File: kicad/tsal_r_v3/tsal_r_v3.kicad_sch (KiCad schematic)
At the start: 48 parts, among them J1 Conn_01x02_Pin, J2 Conn_01x02_Pin, Q1 MMBT3904, Q3 AO3401A, U1 TLV431BQDBZR, U2 NE555D, U3 B1212, U4 2N7002, U7 LTV-817S

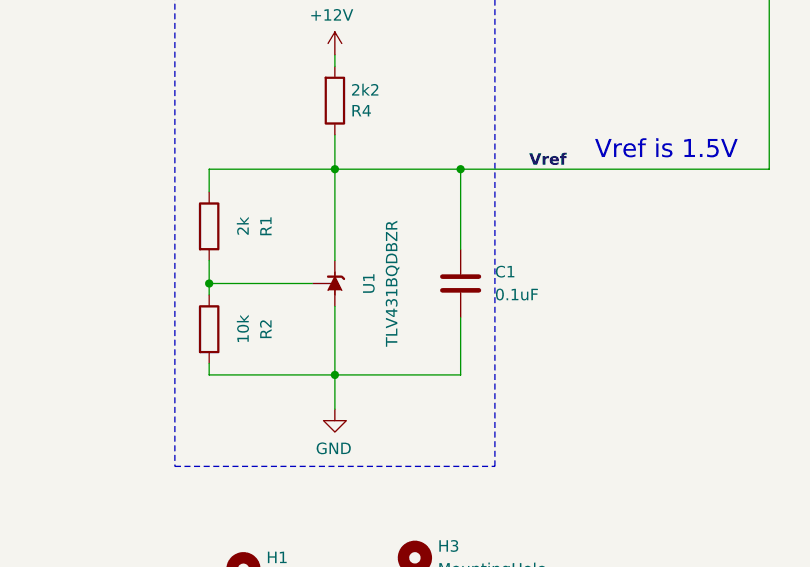
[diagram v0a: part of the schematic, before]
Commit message: TSAL-G v3.0 New PCB design for TSAL-G, with changes for TLV431 for both TSAL-R and TSAL-G
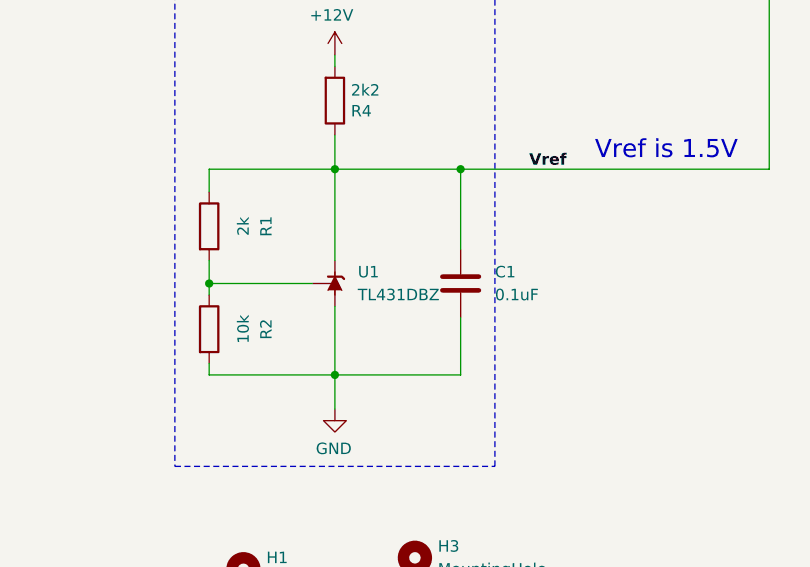
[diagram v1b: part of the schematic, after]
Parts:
- removed U1: TLV431BQDBZR, Package_TO_SOT_SMD:SOT-23, symbol Reference_Voltage:TL431LP
- added U1: TL431DBZ, Package_TO_SOT_SMD:SOT-23, symbol Reference_Voltage:TL431DBZ
- D2: footprint Diode_SMD:D_SMA -> Diode_SMD:D_SMA_Handsoldering
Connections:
- net GND: now also U1.3 (A)
- net Vref: now also U1.1 (K)
- net at R1.2, R2.1: now also U1.2 (REF)

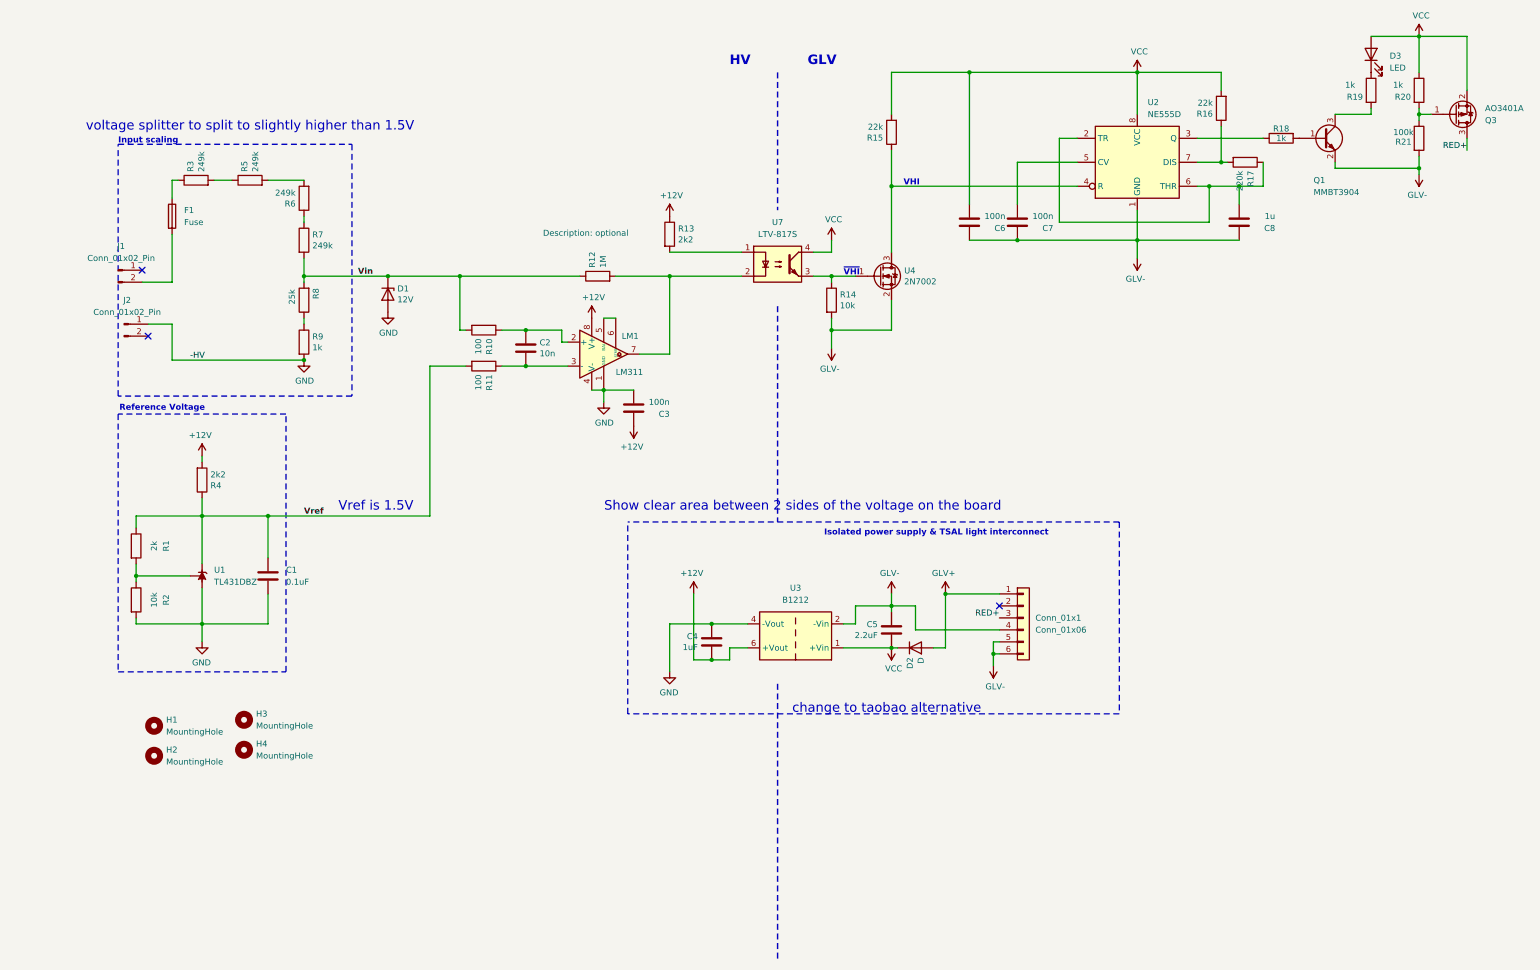
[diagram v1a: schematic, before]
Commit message: change connectors, footprints and new layout
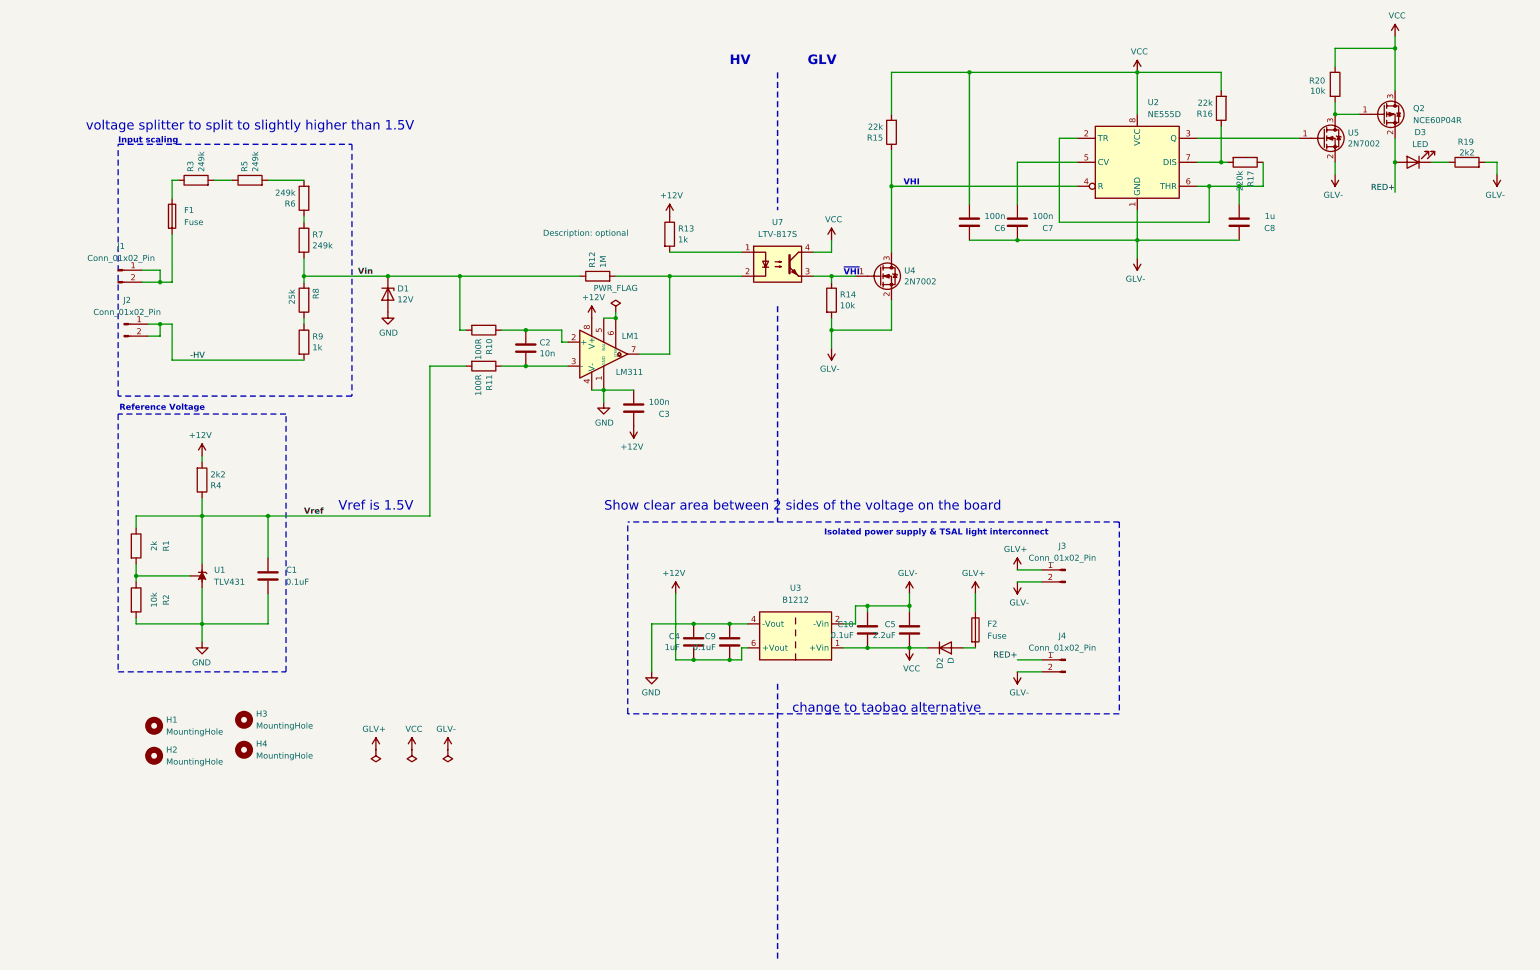
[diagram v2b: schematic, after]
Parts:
- removed Conn_01x1: Conn_01x06, Connector_JST:JST_VH_B6P-VH_1x06_P3.96mm_Vertical, symbol Connector_Generic:Conn_01x06
- removed Q1: MMBT3904, Package_TO_SOT_SMD:SOT-23_Handsoldering, symbol Transistor_BJT:MMBT3904
- removed Q3: AO3401A, Package_TO_SOT_SMD:SOT-23_Handsoldering, symbol Transistor_FET:AO3401A
- removed R18: 1k, Resistor_SMD:R_0805_2012Metric_Pad1.20x1.40mm_HandSolder, symbol Device:R
- removed R21: 100k, Resistor_SMD:R_0805_2012Metric_Pad1.20x1.40mm_HandSolder, symbol Device:R
- added C10, C9: 0.1uF, RMC_Capacitor:C_0805_2012Metric_Pad1.18x1.45mm_HandSolder_L, symbol Device:C
- added F2: Fuse, Fuse:Fuse_1210_3225Metric_Pad1.42x2.65mm_HandSolder, symbol Device:Fuse
- added J3, J4: Conn_01x02_Pin, Connector_Molex:Molex_Micro-Fit_3.0_43650-0200_1x02_P3.00mm_Horizontal, symbol Connector:Conn_01x02_Pin
- added Q2: NCE60P04R, Package_TO_SOT_SMD:SOT-223-3_TabPin2, symbol Transistor_FET:Q_PMOS_GSD
- added U5: 2N7002, RMC_SOT:SOT-23, symbol Transistor_FET:2N7002
- C1, C2, C3, C4, C5, C6, C7, C8: footprint Capacitor_SMD:C_0805_2012Metric_Pad1.18x1.45mm_HandSolder -> RMC_Capacitor:C_0805_2012Metric_Pad1.18x1.45mm_HandSolder_L
- D3: footprint LED_SMD:LED_0805_2012Metric_Pad1.15x1.40mm_HandSolder -> RMC_LED:LED_0805_2012Metric_Pad1.45x1.40mm_HandSolder
- F1: footprint Fuse:Fuse_0805_2012Metric_Pad1.15x1.40mm_HandSolder -> Fuse:Fuse_Littelfuse-NANO2-885
- J1, J2: footprint Connector_AMASS:AMASS_XT60-M_1x02_P7.20mm_Vertical -> Connector_Molex:Molex_Micro-Fit_3.0_43650-0200_1x02_P3.00mm_Horizontal
- LM1, U2: footprint Package_SO:SOIC-8_3.9x4.9mm_P1.27mm -> RMC_SO:SOIC-8_3.9x4.9mm_P1.27mm_RMC_Handsolder
- R1, R12, R14, R15, R16, R17, R2, R3, R4, R5, R6, R7, R8, R9: footprint Resistor_SMD:R_0805_2012Metric_Pad1.20x1.40mm_HandSolder -> RMC_Resistor:R_0805_2012Metric_Pad1.20x1.40mm_HandSolder_L
- R10, R11: value 100 -> 100R; footprint Resistor_SMD:R_0805_2012Metric_Pad1.20x1.40mm_HandSolder -> RMC_Resistor:R_0805_2012Metric_Pad1.20x1.40mm_HandSolder_L
- R13: value 2k2 -> 1k; footprint Resistor_SMD:R_0805_2012Metric_Pad1.20x1.40mm_HandSolder -> RMC_Resistor:R_0805_2012Metric_Pad1.20x1.40mm_HandSolder_L
- R19: value 1k -> 2k2; footprint Resistor_SMD:R_0805_2012Metric_Pad1.20x1.40mm_HandSolder -> RMC_Resistor:R_0805_2012Metric_Pad1.20x1.40mm_HandSolder_L
- R20: value 1k -> 10k; footprint Resistor_SMD:R_0805_2012Metric_Pad1.20x1.40mm_HandSolder -> RMC_Resistor:R_0805_2012Metric_Pad1.20x1.40mm_HandSolder_L
- U1: value TL431DBZ -> TLV431; footprint Package_TO_SOT_SMD:SOT-23 -> RMC_SOT:SOT-23
- U3: footprint Converter_DCDC:Converter_DCDC_TRACO_TBA2-xxxx_Single_THT -> Matthew:DCDC Converter F1212
- U4: footprint Package_TO_SOT_SMD:SOT-23_Handsoldering -> RMC_SOT:SOT-23
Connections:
- net +12V: now also C9.2
- net GLV+: now also F2.1, J3.1 (Pin_1); no longer D2.2 (A)
- net GLV-: now also R19.2, C10.1, J3.2 (Pin_2), J4.2 (Pin_2), U5.2 (S)
- net GND: now also C9.1; no longer J2.1 (Pin_1), R9.2
- net RED+: now also D3.2 (A), J4.1 (Pin_1), Q2.2 (S)
- net VCC: now also C10.2, Q2.3 (D); no longer D3.2 (A)
- net at U2.3 (Q): now also U5.1 (G)
- net at R20.2: now also Q2.1 (G), U5.3 (D)
- net at J1.1 (Pin_1): now also F1.2, J1.2 (Pin_2)
- net -HV: now reaches J2.2 (Pin_2)
- net -HV: now also J2.1 (Pin_1), R9.2
- new net: D2.2 (A), F2.2
- no-connect marks 3 -> 0
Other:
- moved on the sheet: C4, C5, D2, R20

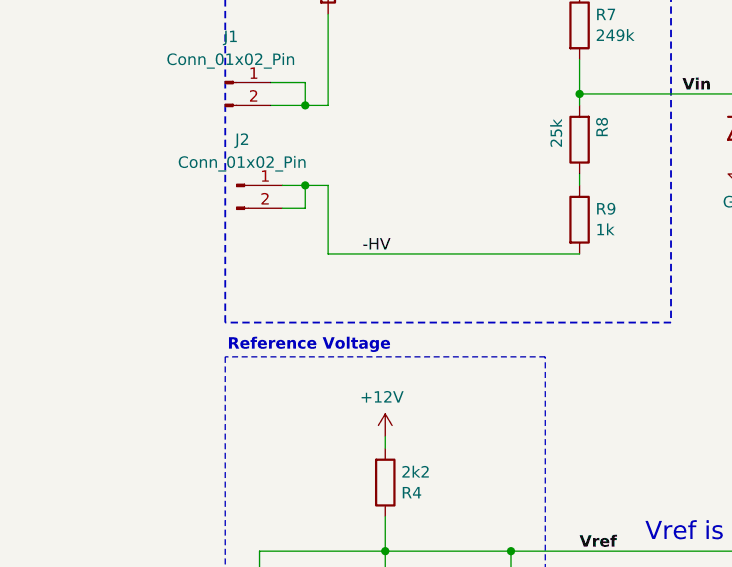
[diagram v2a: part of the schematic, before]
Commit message: Debugged tsal r
inverted tlv431 pad
connected hv- gnd
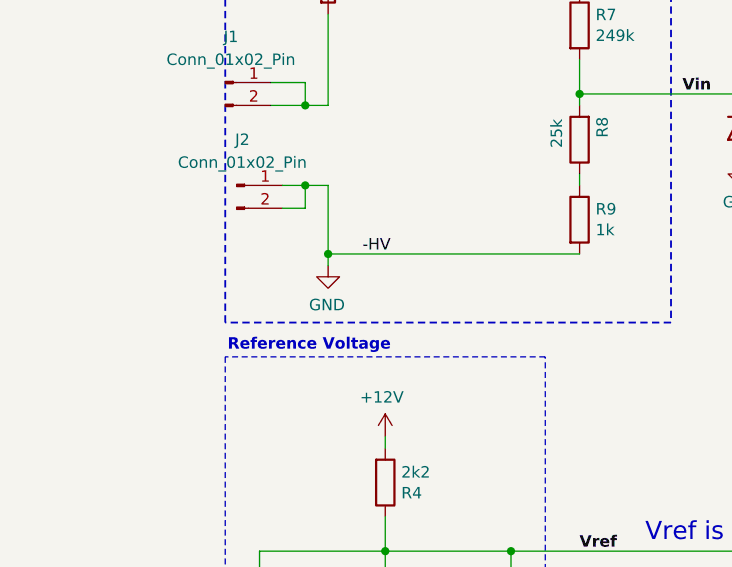
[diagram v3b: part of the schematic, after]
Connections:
- net -HV is gone; now on net GND: J2.1 (Pin_1), J2.2 (Pin_2), R9.2
- net Vref: now also U1.2 (K); no longer U1.1 (K)
- net at R1.2, R2.1: now also U1.1 (REF); no longer U1.2 (REF)
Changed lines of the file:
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@@
 	)
 	(junction
+		(at 72.39 146.05)
+		(diameter 0)
+		(color 0 0 0 0)
+	)
+	(junction
 		(at 228.6 198.12)
 		(diameter 0)
@@
 	(wire
 		(pts
+			(xy 72.39 147.32) (xy 72.39 146.05)
+		)
+		(stroke
+			(width 0)
+			(type default)
+		)
+	)
+	(wire
+		(pts
 			(xy 166.37 135.89) (xy 166.37 137.16)
 		)
@@
 					(unit 1)
 				)
+			)
+		)
+	)
+	(symbol
+		(lib_id "power:GND")
+		(at 72.39 147.32 0)
+		(mirror y)
+		(unit 1)
+		(exclude_from_sim no)
+		(in_bom yes)
+		(on_board yes)
+		(dnp no)
+		(property "Reference" "#PWR026"
+			(at 72.39 153.67 0)
+			(effects
+				(font
+					(size 1.27 1.27)
+				)
+				(hide yes)
+			)
+		)
+		(property "Value" "GND"
+			(at 72.263 151.7142 0)
+			(effects
+				(font
+					(size 1.27 1.27)
+				)
+			)
+		)
+		(property "Footprint" ""
+			(at 72.39 147.32 0)
+			(effects
+				(font
+					(size 1.27 1.27)
+				)
+				(hide yes)
+			)
+		)
+		(property "Datasheet" ""
+			(at 72.39 147.32 0)
+			(effects
+				(font
+					(size 1.27 1.27)
+				)
+				(hide yes)
+			)
+		)
+		(property "Description" ""
+			(at 72.39 147.32 0)
+			(effects
+				(font
+					(size 1.27 1.27)
+				)
+				(hide yes)
+			)
+		)
+		(pin "1"
+		)
+		(instances
+			(project "tsal_r_v3"
+				(path "/94e47eea-ee3d-40f5-84ad-e3510a82a1d2"
+					(reference "#PWR026")
+					(unit 1)
+				)

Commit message: tsalR
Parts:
- Q2: footprint Package_TO_SOT_SMD:SOT-223-3_TabPin2 -> RMC_TO:TO-252-2
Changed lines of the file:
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@@
 			)
 		)
-		(property "Footprint" "Package_TO_SOT_SMD:SOT-223-3_TabPin2"
+		(property "Footprint" "RMC_TO:TO-252-2"
 			(at 334.01 91.44 0)
 			(effects
